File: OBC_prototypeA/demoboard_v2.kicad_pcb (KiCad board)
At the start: 2 copper layers, 95.9 x 90.2 mm, 129 parts, among them J1 PC104-8BIT, P1 3v3_IN_CONNECTOR, P10 FLASH_CS, P11 USB_5V, P12 JTAG_20PIN, P13 WD_EN, P2 INA_INPUT, P3 INA_GND, P4 INA_EN, P5 INA_OUTPUT, P6 USB_PORT, P7 OSC_FUALT_INJECT, P8 RTC_SPI, P9 FLASH_SPI, Q1 DMN2075U, Q2 DMN2075U, Q3 1v2_GOOD, Q4 DMN2075U, Q5 DMN2075U, SW1 SPST, SW2 SPST, U1 TMS570LS0714, U10 FT230XQ-R, U2 AP7331, U3 AP7361_3.3v, U4 INA301, U5 FLASH_IS25LP016D, U6 FLASH_IS25LP016D, U7 FLASH_IS25LP016D, U8 AB-RTCMC-EOA9-S3, U9 TPS3110, Y1 XTAL

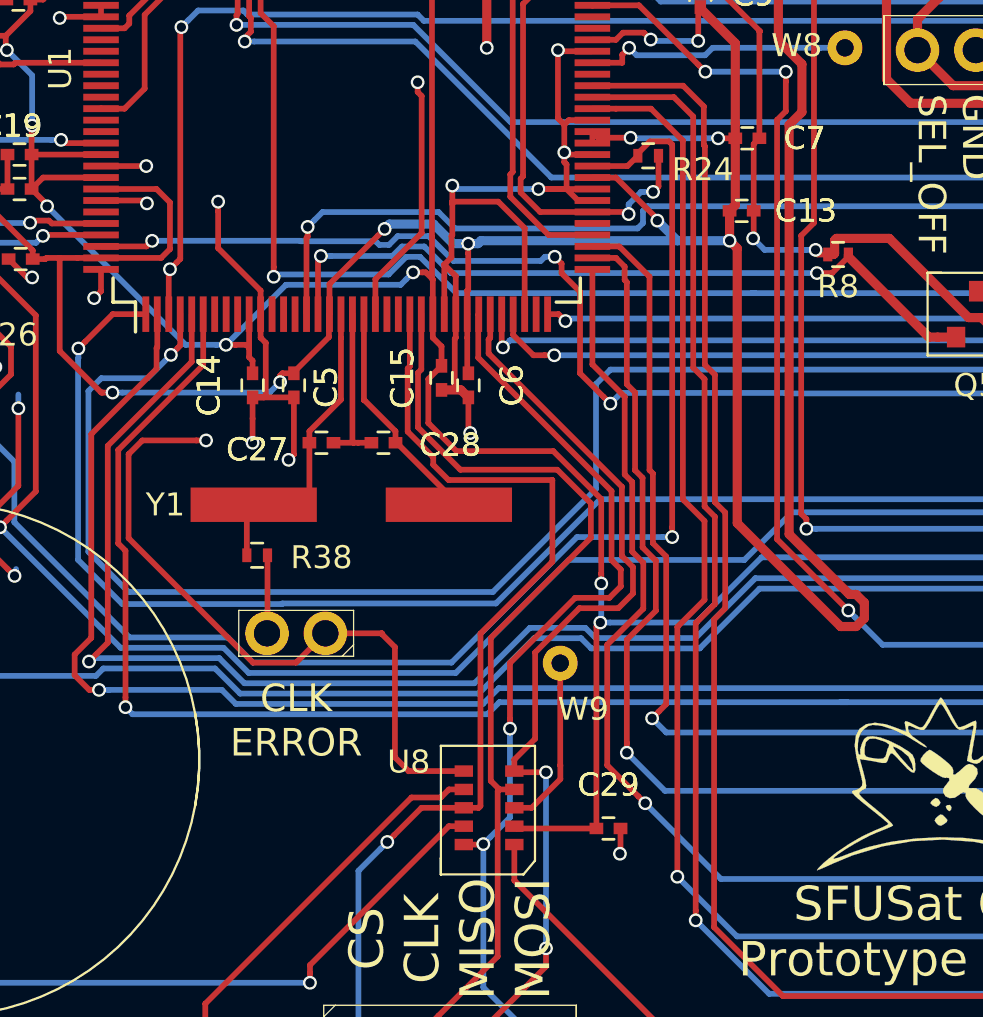
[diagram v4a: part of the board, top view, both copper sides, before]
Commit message: Cleaned up oscillator traces
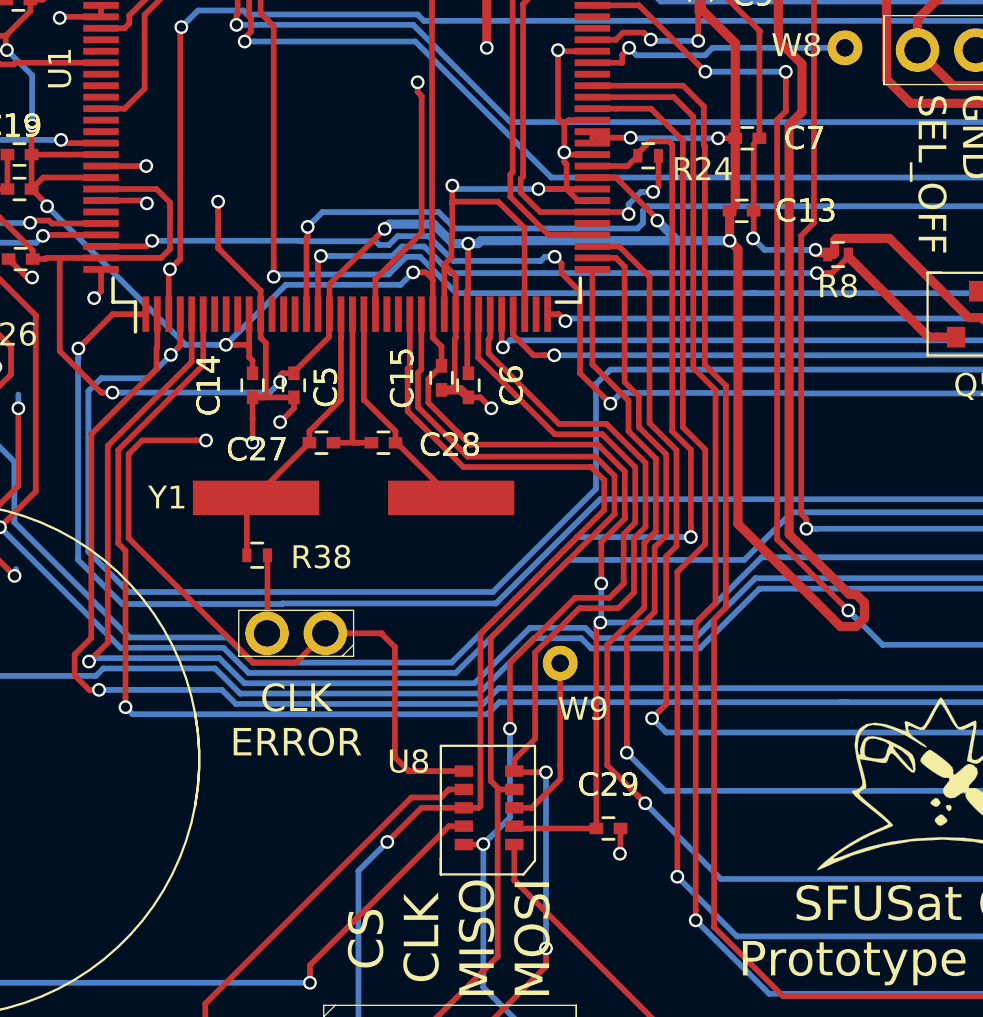
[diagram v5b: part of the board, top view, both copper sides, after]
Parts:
- moved Y1 0.32 mm to (138.3, 81.7)
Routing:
- net RTC_CS: track 41.8 -> 44.3 mm
- net 3v3: track 397.7 -> 400.2 mm
- net GND: track 218.7 -> 216.9 mm
- net RTC_MOSI: track 39.2 -> 40.9 mm
- net RTC_MISO: track 39.9 -> 41.6 mm
- net RTC_CLK: track 41.3 -> 42.9 mm
- net Net-(C27-Pad1): track 13.4 -> 12.2 mm
- net MASTER_RESET: track 199.0 -> 200.2 mm

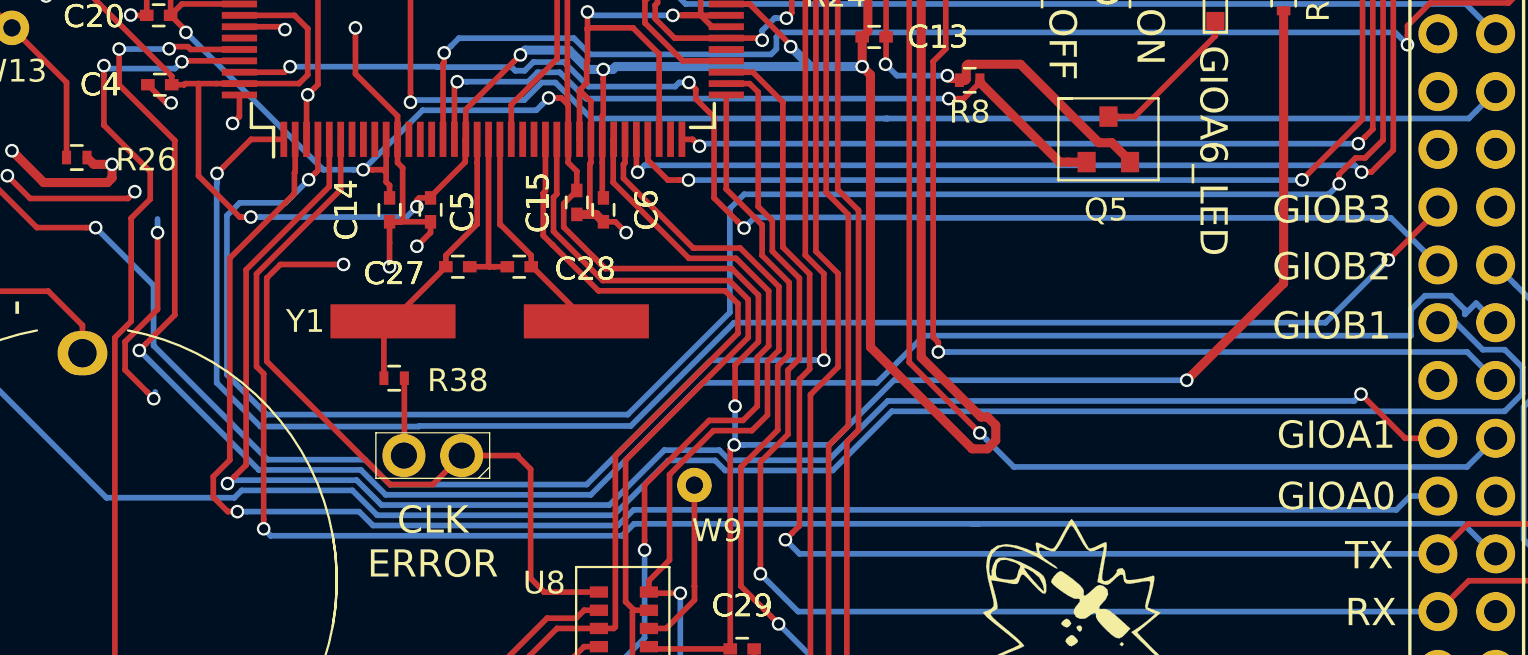
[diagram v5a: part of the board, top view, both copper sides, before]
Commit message: Removed gnd plane from under oscillator, added differential oscillator signal. Generated gerbers
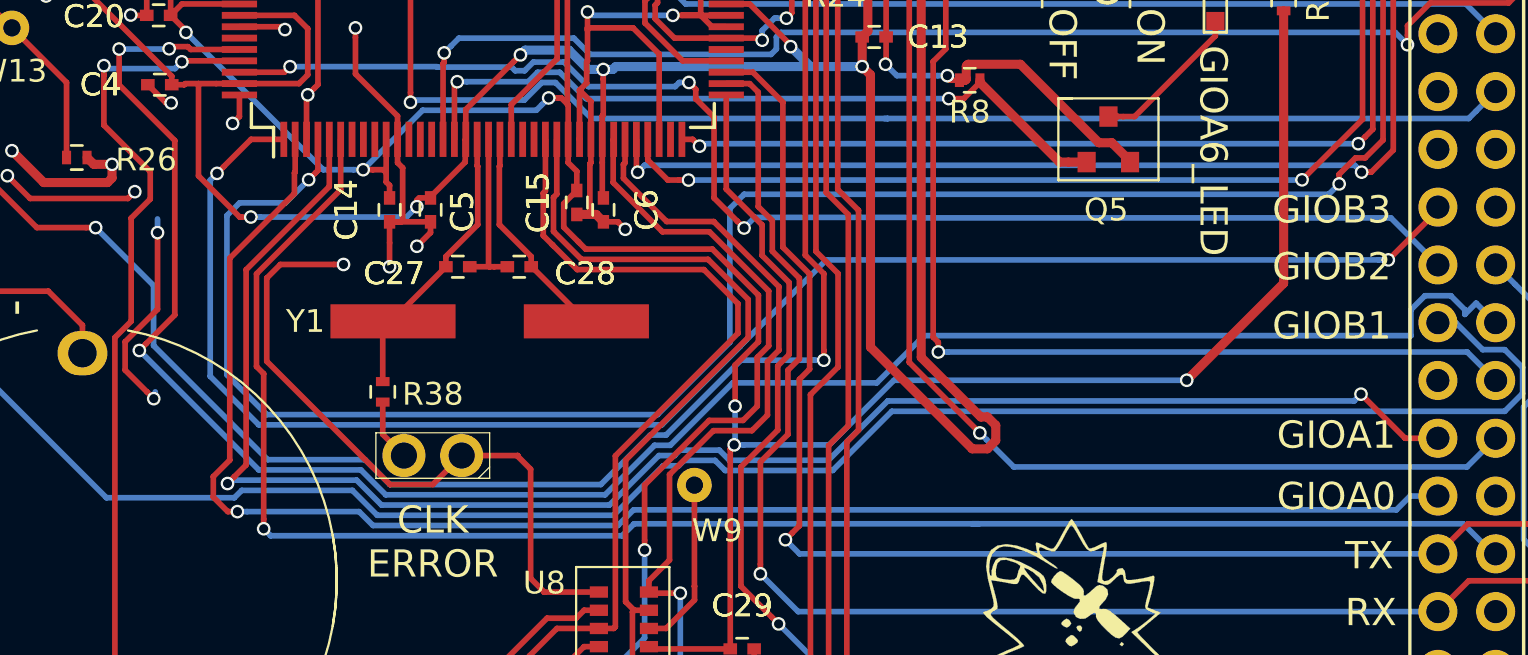
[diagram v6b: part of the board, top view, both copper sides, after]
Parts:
- moved R38 0.78 mm to (133.6, 84.8), turned to 270 degrees
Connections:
- net Net-(C27-Pad1) renamed /MCU_Support_Reset/OSC_P
- net Net-(C28-Pad2) renamed /MCU_Support_Reset/OSC_N
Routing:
- net I2C_SDA: track 83.4 -> 84.2 mm
- net 3v3: track 400.2 -> 399.4 mm
- net /MCU_Support_Reset/OSC_P: track 12.2 -> 13.0 mm
- net Net-(P7-Pad2): track 3.91 -> 3.27 mm

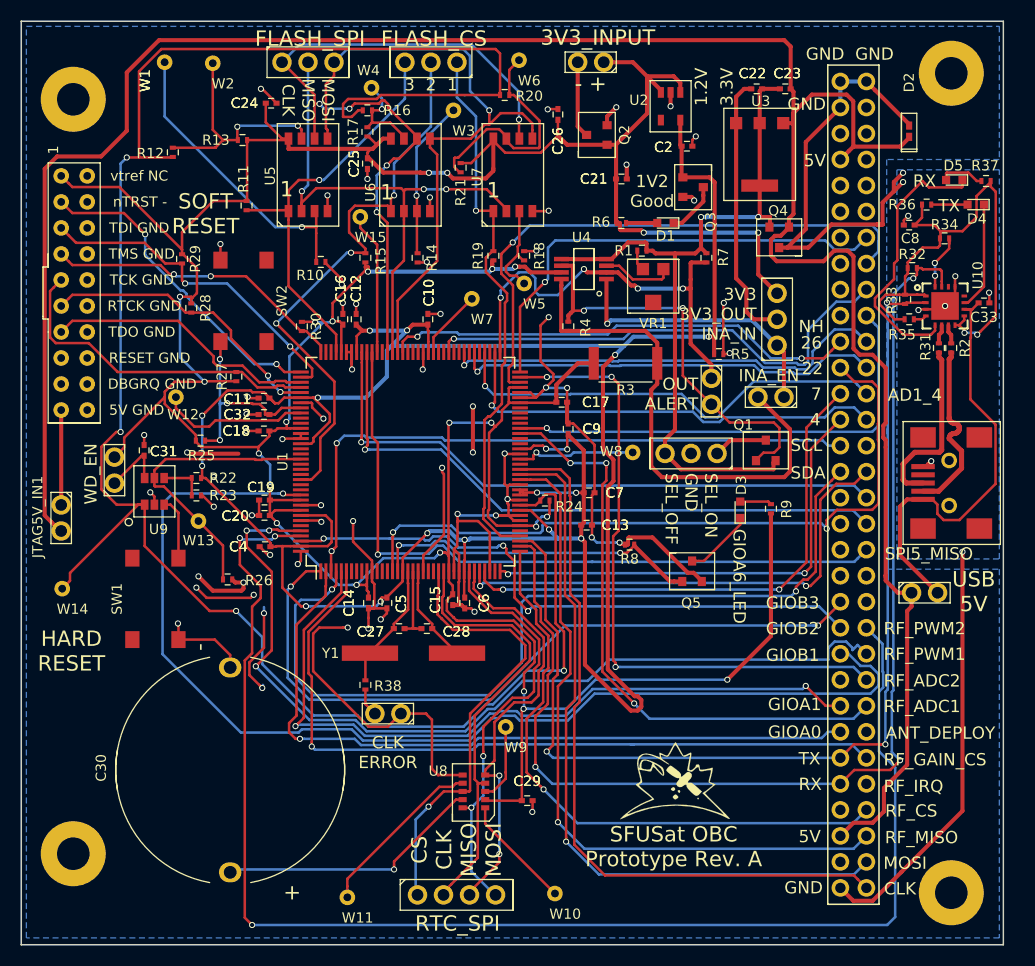
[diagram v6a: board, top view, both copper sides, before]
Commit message: Cleaned up some floating traces and silkscreens. Generated gerbers for board house
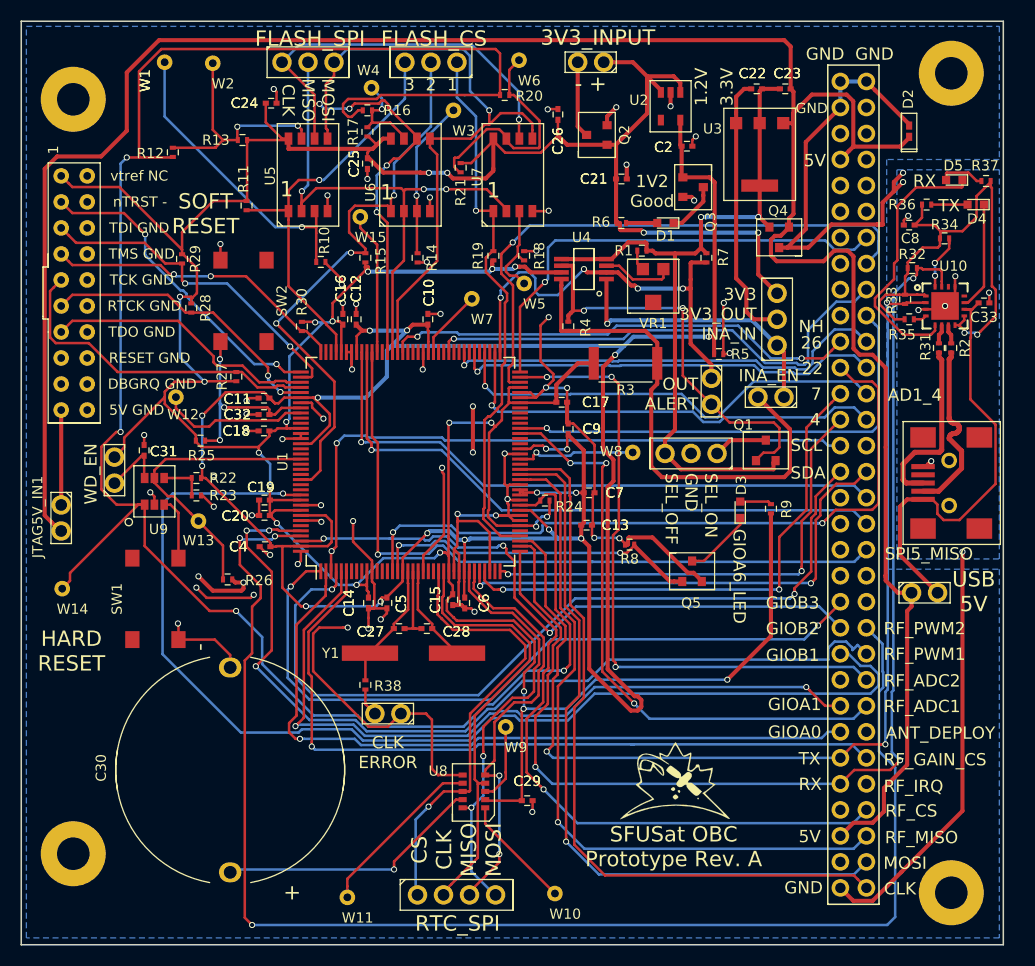
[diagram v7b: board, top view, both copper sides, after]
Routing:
- net (no net): track 25.2 -> 10.9 mm, vias 8 -> 5
- net I2C_SDA: track 84.2 -> 80.6 mm
- net GIOB2: track 60.4 -> 62.1 mm
- net NHET1_22: track 70.1 -> 69.1 mm
- net GND: track 216.8 -> 216.0 mm
- net RF_CS: track 59.4 -> 60.0 mm
- net UART_RX: track 115.4 -> 116.0 mm
- net UART_TX: track 104.6 -> 105.3 mm
- net 104_GND: track 73.7 -> 73.1 mm
- net SPI5_MOSI: track 61.6 -> 61.1 mm
- net Net-(D5-Pad1): track 26.7 -> 26.2 mm
